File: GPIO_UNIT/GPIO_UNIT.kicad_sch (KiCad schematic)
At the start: 0 parts

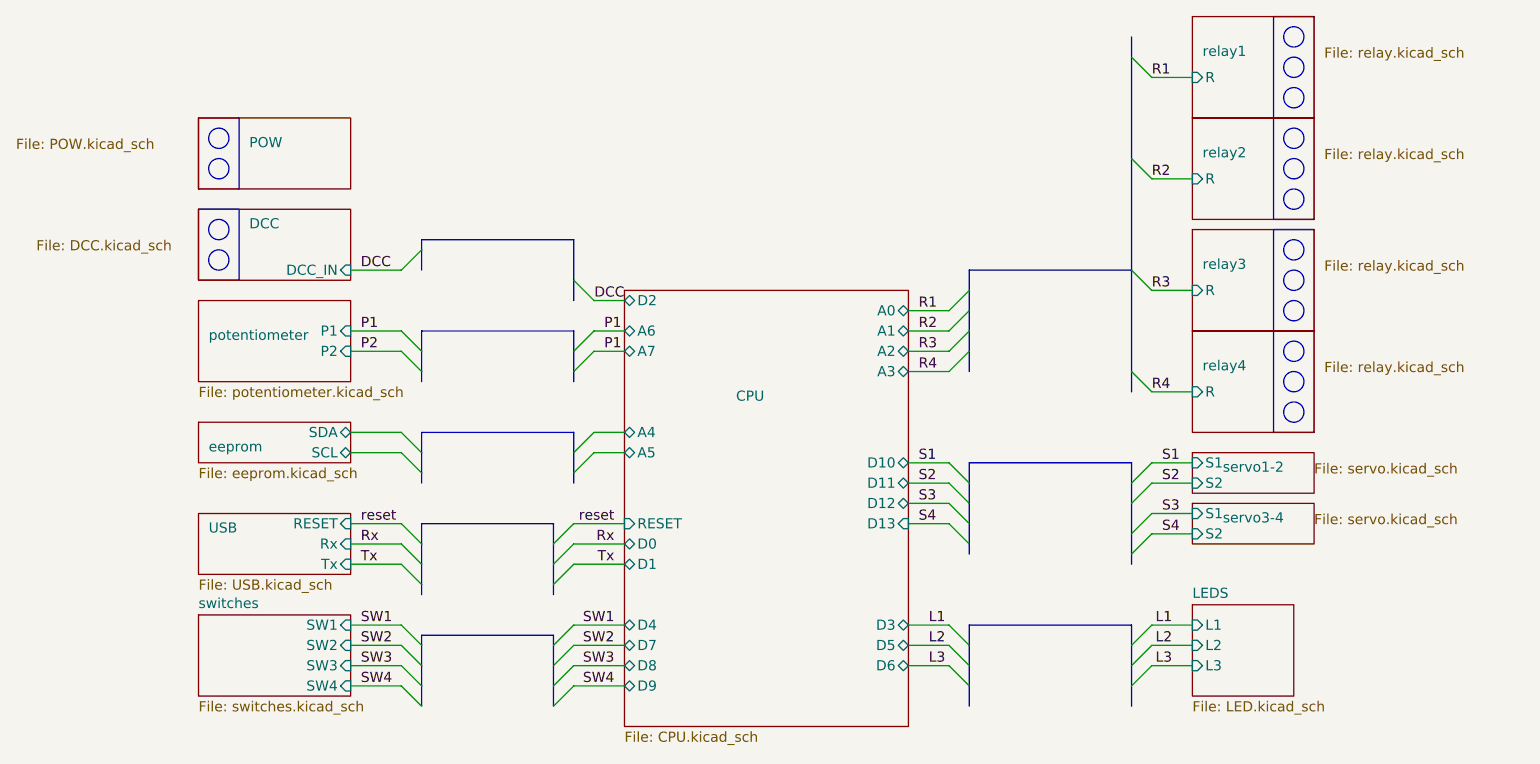
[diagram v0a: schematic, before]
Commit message: Digital pins are now able to use the analog pinnumbering as well. Pin can be set to an analog or digital pin number by simply pressing a or d respectively when editting the pinnumbers. Take note that one can fill in invalid analog pinnumbers. Also due to me support the arduino mega, I should remove pin number limit all togather.
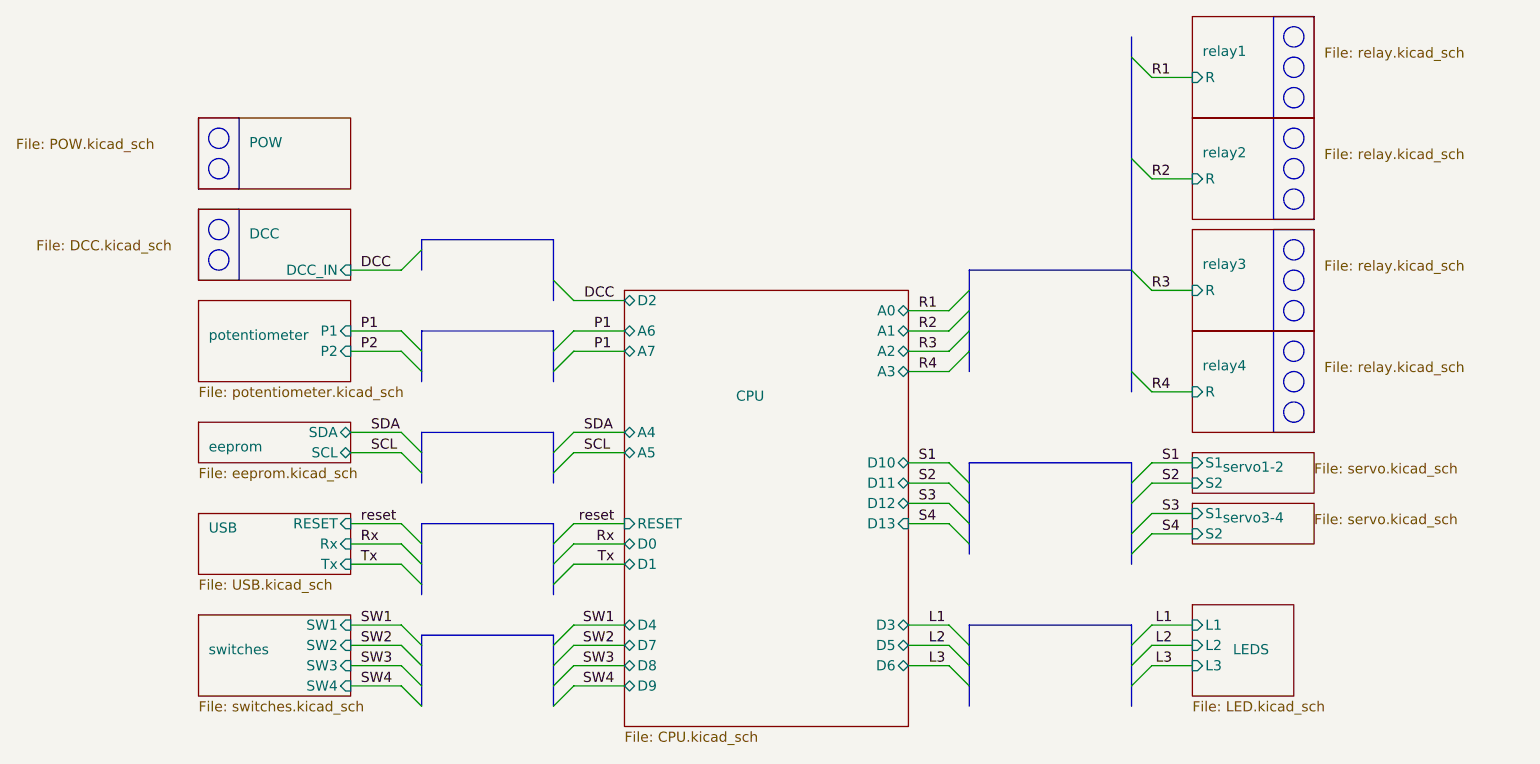
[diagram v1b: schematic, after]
